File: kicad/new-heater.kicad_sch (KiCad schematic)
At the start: 19 parts, among them J1 USB connector, J3 To SHT40 module, M1 Fan, Q1 AO3400A, Q2 IRLZ34N, U1 BP

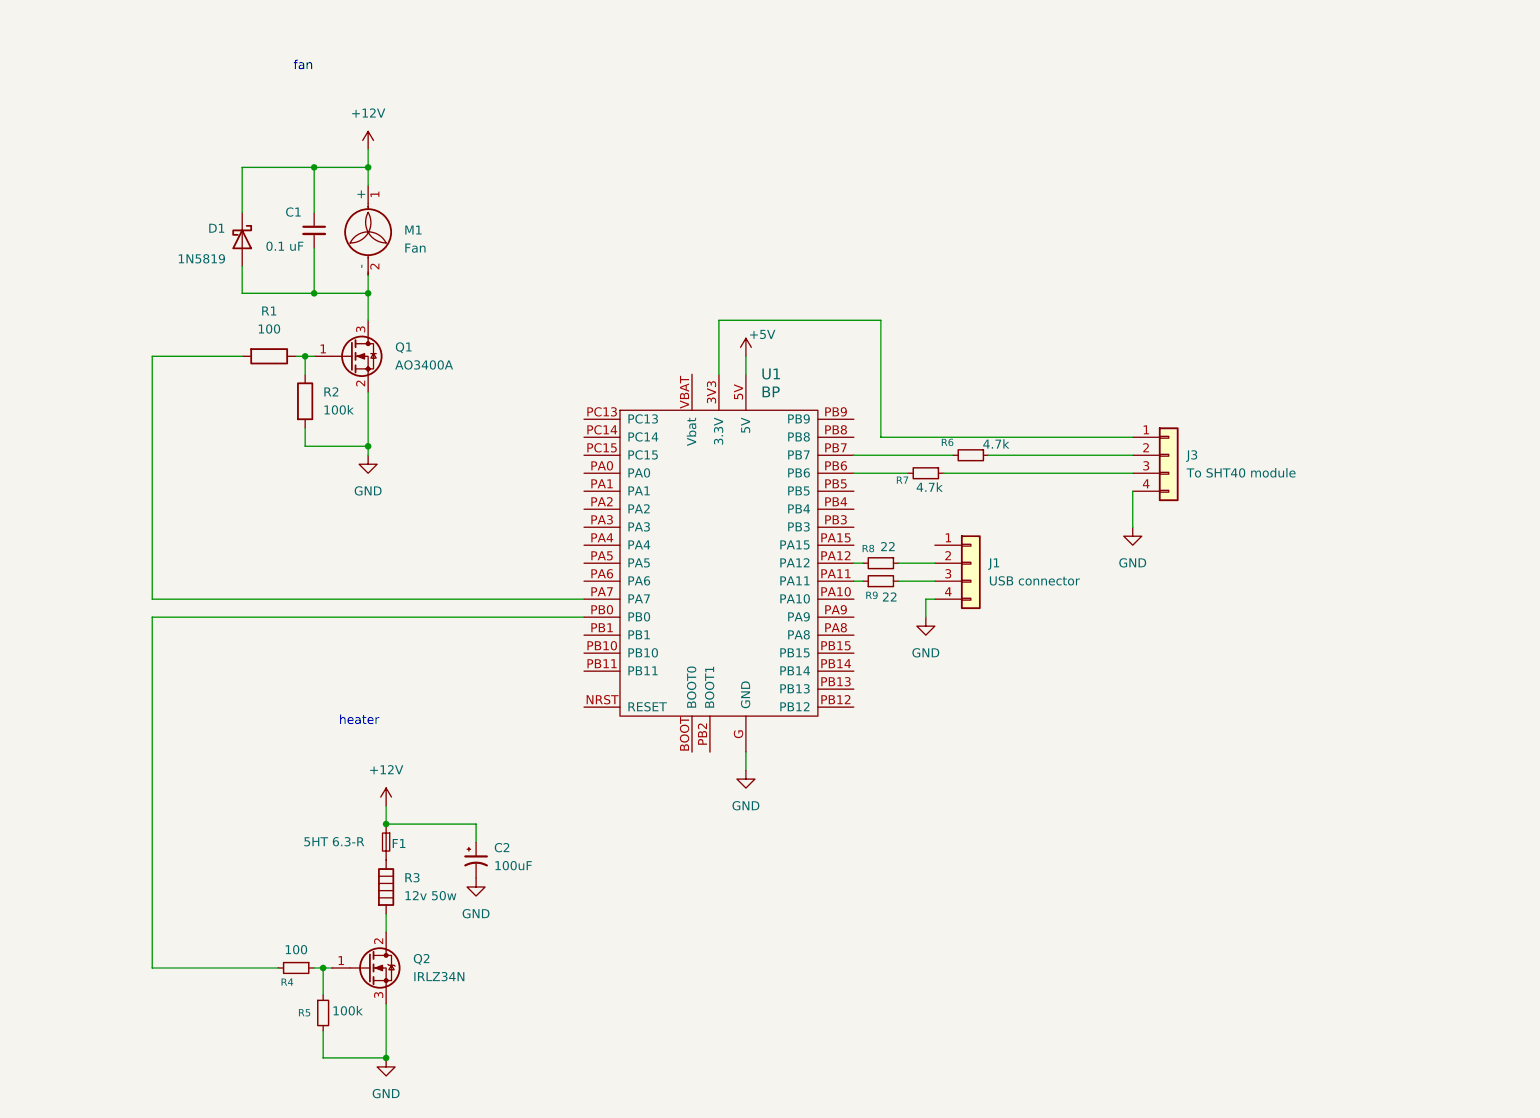
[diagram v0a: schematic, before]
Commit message: updated schematic with fet driver and connectors instead of heater/fan
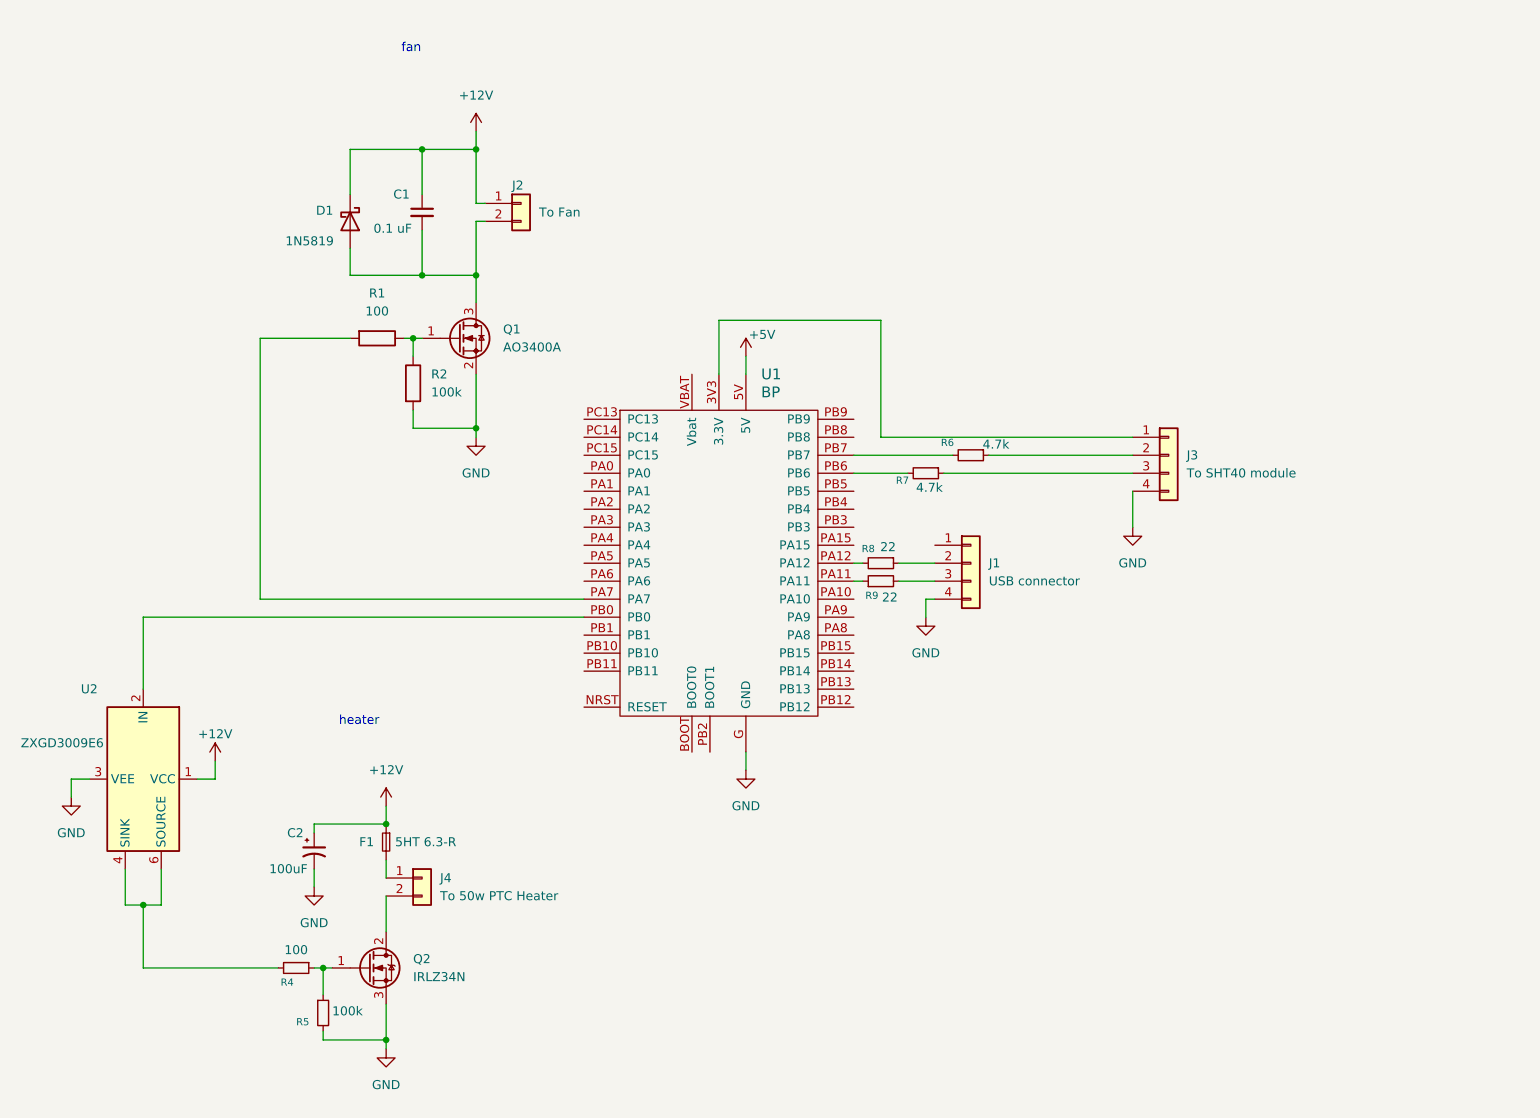
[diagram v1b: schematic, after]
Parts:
- removed M1: Fan, symbol Motor:Fan
- removed R3: 12v 50w, symbol Device:Heater
- added J2: To Fan, symbol Connector_Generic:Conn_01x02
- added J4: To 50w PTC Heater, symbol Connector_Generic:Conn_01x02
- added U2: ZXGD3009E6, Package_TO_SOT_SMD:SOT-23-6, symbol Driver_FET:ZXGD3009E6
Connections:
- net +12V: now also J2.1 (Pin_1), U2.1 (VCC)
- net GND: now also U2.3 (VEE)
- net at C1.2, D1.2 (A), Q1.3 (D): now also J2.2 (Pin_2)
- net at U1.PB0: now also U2.2 (IN); no longer R4.2
- net at Q2.2 (D): now also J4.2 (Pin_2)
- net at F1.2: now also J4.1 (Pin_1)
- new net: R4.2, U2.4 (SINK), U2.6 (SOURCE)
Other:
- moved on the sheet: C1, C2, D1, Q1, R1, R2

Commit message: added power supply filtering, moved fuse to input
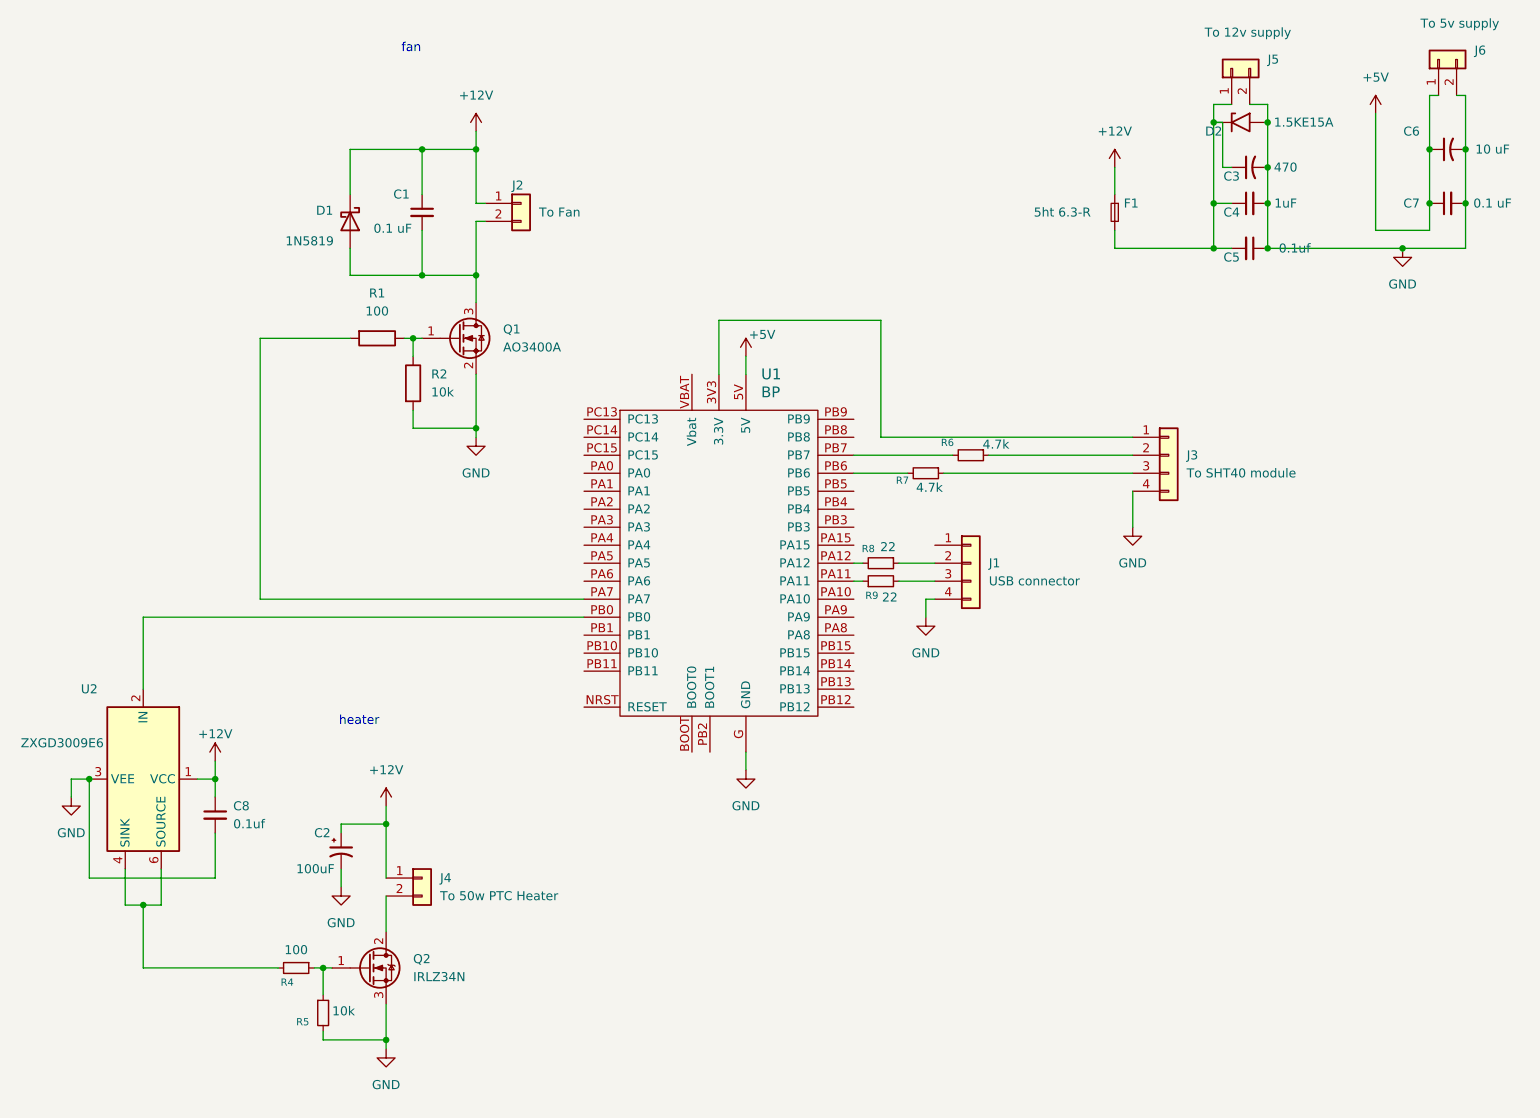
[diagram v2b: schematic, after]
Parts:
- added C3: 470, symbol Device:C_Small_US
- added C4: 1uF, symbol Device:C_Small
- added C5, C8: 0.1uf, symbol Device:C_Small
- added C6: 10 uF, symbol Device:C_Small_US
- added C7: 0.1 uF, symbol Device:C_Small
- added D2: 1.5KE15A, Diode_THT:D_DO-201AE_P15.24mm_Horizontal, symbol Diode:1.5KExxA
- added J5: To 12v supply, symbol Connector_Generic:Conn_01x02
- added J6: To 5v supply, symbol Connector_Generic:Conn_01x02
- F1: value 5HT 6.3-R -> 5ht 6.3-R
- R2, R5: value 100k -> 10k
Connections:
- net +12V: now also J4.1 (Pin_1), C8.1
- net +5V: now also C6.1, C7.1, J6.1 (Pin_1)
- net GND: now also C3.2, C4.2, C5.1, C6.2, C7.2, C8.2, D2.2 (A2), J5.2 (Pin_2), J6.2 (Pin_2)
- net at F1.2: now also C3.1, C4.1, C5.2, D2.1 (A1), J5.1 (Pin_1); no longer J4.1 (Pin_1)
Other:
- moved on the sheet: C2
